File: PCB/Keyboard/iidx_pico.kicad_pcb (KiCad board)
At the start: 2 copper layers, 180 x 160 mm, 79 parts, among them J1 Spin, J2 Spin, J3 RGB, J4 RGB, J5 Spin, J6 Spin, SW1 SWITCH_SPST, SW10 SWITCH_SPST, SW11 SWITCH_SPST, SW12 Tact_4pin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

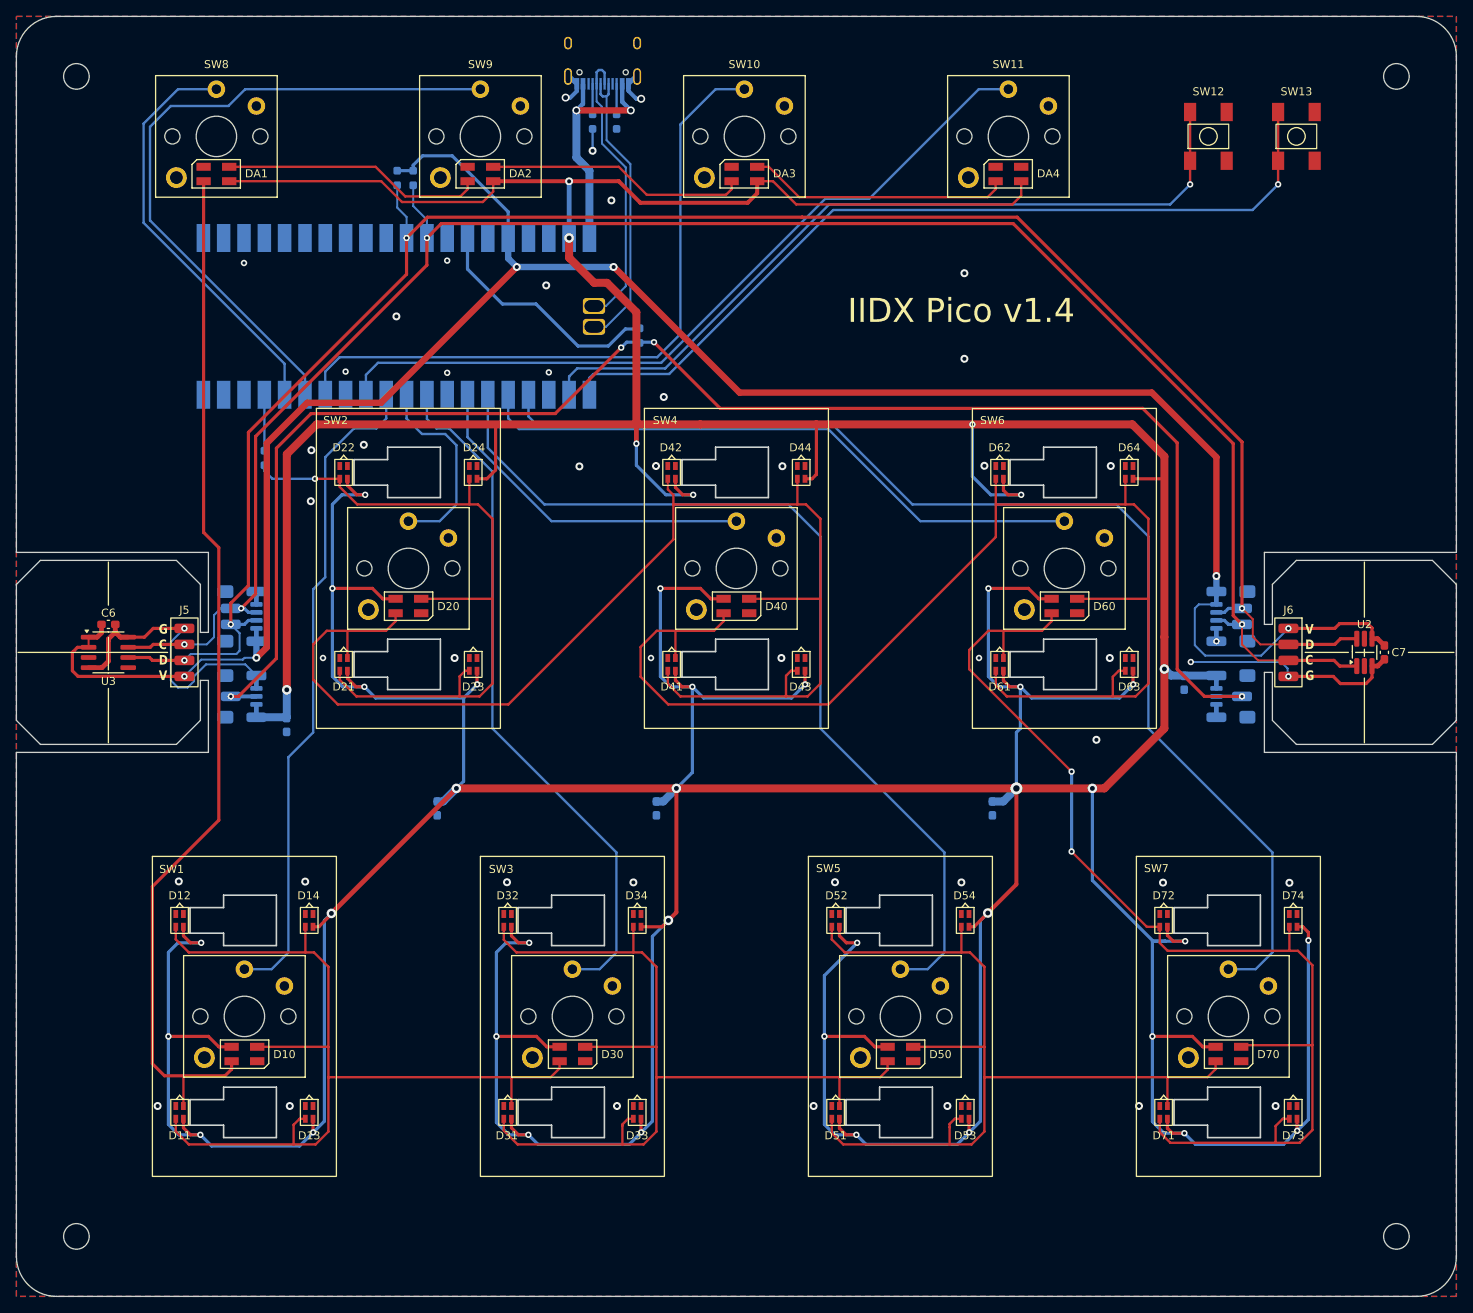
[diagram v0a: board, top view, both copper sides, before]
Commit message: PCB v1.41 (better 1615 LED footprint)
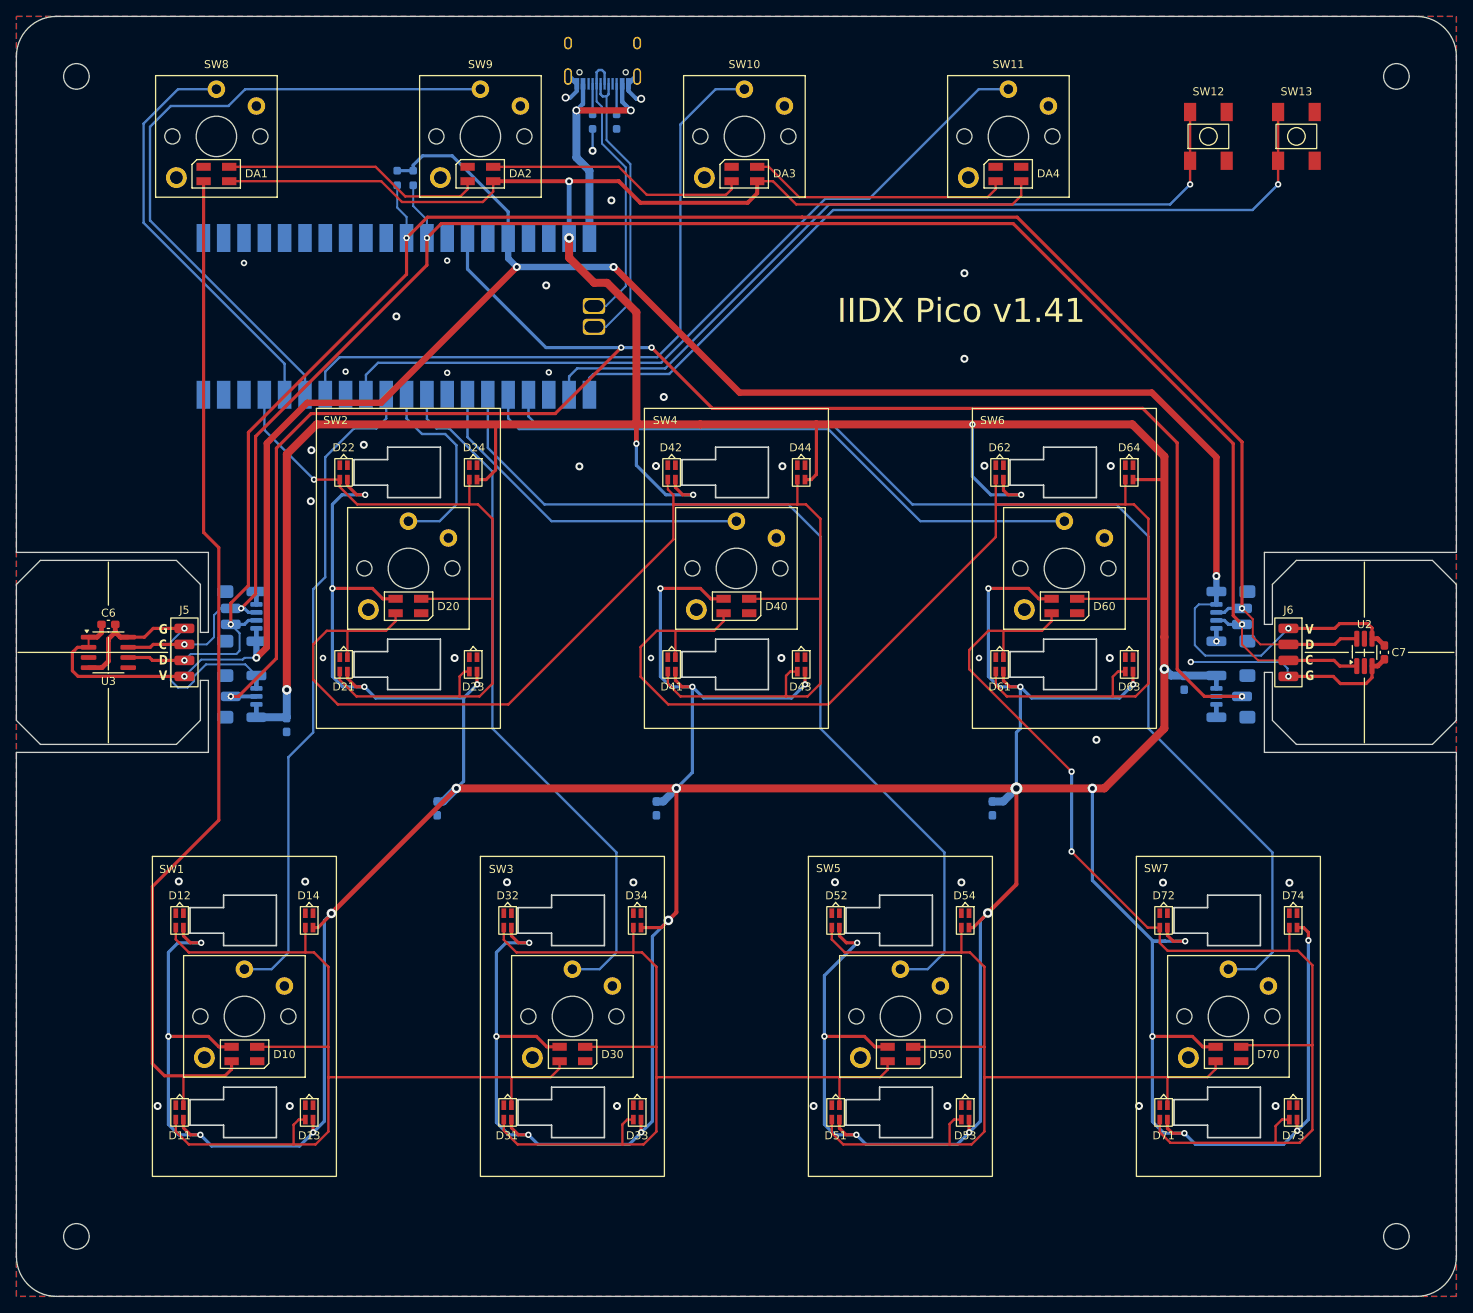
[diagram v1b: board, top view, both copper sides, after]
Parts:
- removed the R1 at (78.3, 74.6)
- removed the R2 at (125.2, 59.3)
- renumbered R20 to R1, R21 to R2
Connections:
- U1 pad 17: Net-(U1-GPIO13) -> /LED2
- U1 pad 34: Net-(U1-GPIO28_ADC2) -> /TT_LED
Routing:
- net Net-(U1-GPIO28_ADC2): track 30.3 -> 0.00 mm
- net /TT_LED: track 201.4 -> 228.1 mm
- net Net-(U1-GPIO13): track 7.90 -> 0.00 mm
- net /LED2: track 90.7 -> 97.1 mm
- net +5V: track 1137.9 -> 1136.0 mm
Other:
- board text added: "IIDX Pico v1.41"
- board text removed: "IIDX Pico v1.4"
